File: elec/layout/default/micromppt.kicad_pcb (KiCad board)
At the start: 2 copper layers, 25.7 x 15.1 mm, 20 parts, among them U5 10µF ±10% 10V X5R, U6 10kΩ ±1% 62.5mW

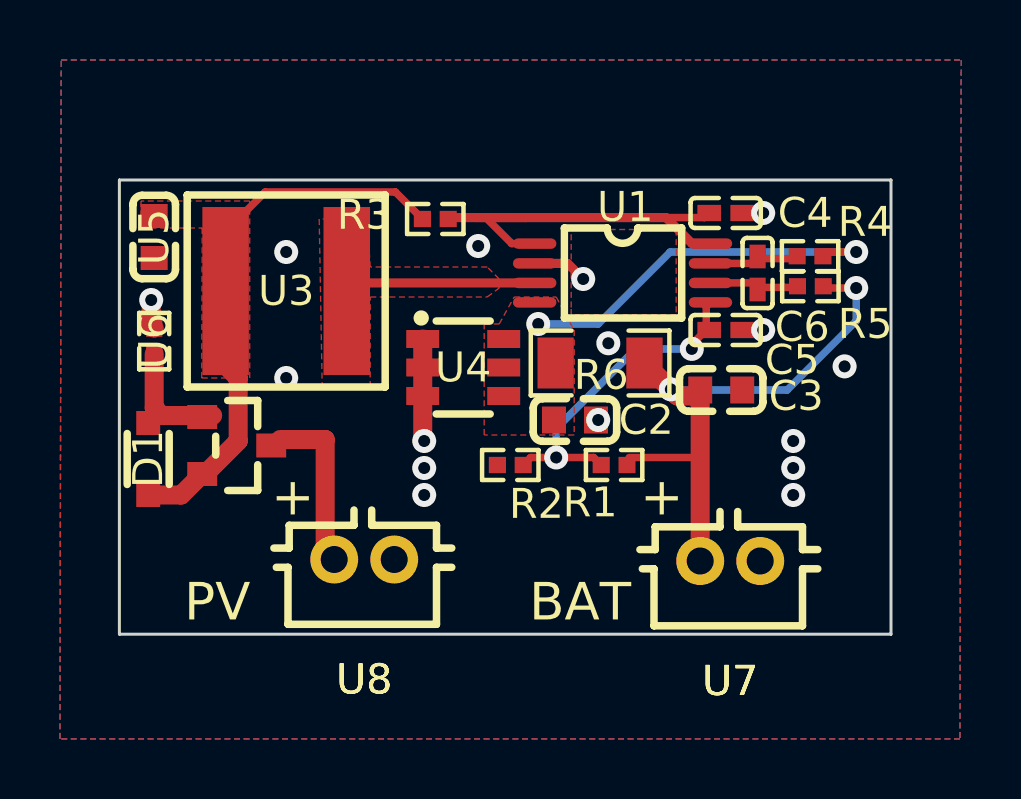
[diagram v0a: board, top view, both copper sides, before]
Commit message: fixed .github/workflows/ci.yml and set github actions versions to v4
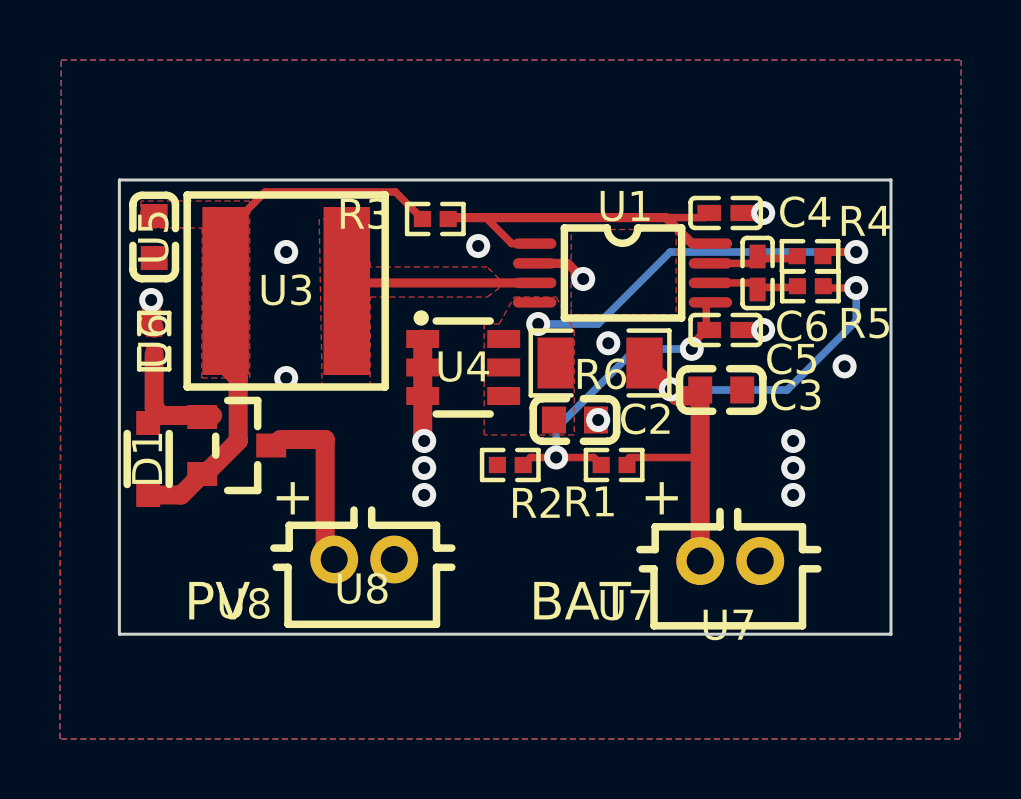
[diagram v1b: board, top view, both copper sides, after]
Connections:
- net S renamed C
- net VOUT renamed cathode
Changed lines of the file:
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@@
     (net 3 "ICTRL_PLUS")
     (net 4 "LX")
-    (net 5 "VOUT")
+    (net 5 "cathode")
     (net 6 "VCTRL")
     (net 7 "G")
-    (net 8 "S")
+    (net 8 "C")
     (net 9 "hv")
     (net 10 "gnd")
@@
             (size 1.1 0.6)
             (layers "F.Cu" "F.Mask" "F.Paste")
-            (net 5 "VOUT")
+            (net 5 "cathode")
             (pintype "stereo")
         )
@@
             (size 1.1 0.6)
             (layers "F.Cu" "F.Mask" "F.Paste")
-            (net 5 "VOUT")
+            (net 5 "cathode")
             (pintype "stereo")
         )
@@
             (size 1.1 0.6)
             (layers "F.Cu" "F.Mask" "F.Paste")
-            (net 5 "VOUT")
+            (net 5 "cathode")
             (pintype "stereo")
         )
@@
         (at 74.6 55.65 180)
         (property "Reference" "U8"
-            (at 0 -4 0)
+            (at 4 -1.5 0)
             (layer "F.SilkS")
             (hide no)
@@
             (layer "F.SilkS")
         )
-        (fp_line
-            (start 3 1.7)
-            (end -3 1.7)
-            (stroke
-                (width 3)
-                (type solid)
-            )
-            (layer "F.Fab")
-        )
-        (fp_line
-            (start 3 -2.8)
-            (end 3 1.7)
-            (stroke
-                (width 3)
-                (type solid)
-            )
-            (layer "F.Fab")
-        )
-        (fp_line
-            (start -3 -2.8)
-            (end 3 -2.8)
-            (stroke
-                (width 3)
-                (type solid)
-            )
-            (layer "F.Fab")
-        )
-        (fp_line
-            (start -3 -2.8)
-            (end -3 -2.8)
-            (stroke
-                (width 3)
-                (type solid)
-            )
-            (layer "F.Fab")
-        )
         (fp_circle
             (center 2.95 -2.8)
@@
         )
         (fp_text user "${REFERENCE}"
-            (at 0 -4 0)
+            (at 0.065 -1 0)
             (layer "F.SilkS")
             (effects
@@
             (size 0.8 0.9)
             (layers "F.Cu" "F.Mask" "F.Paste")
-            (net 8 "S")
+            (net 8 "C")
         )
         (pad "2" smd rect
@@
         (at 86.8 55.7 180)
         (property "Reference" "U7"
-            (at 0 -4 0)
+            (at 3.5 -1.5 0)
             (layer "F.SilkS")
             (hide no)
@@
             (layer "F.SilkS")
         )
-        (fp_line
-            (start 3 1.7)
-            (end -3 1.7)
-            (stroke
-                (width 3)
-                (type solid)
-            )
-            (layer "F.Fab")
-        )
-        (fp_line
-            (start 3 -2.8)
-            (end 3 1.7)
-            (stroke
-                (width 3)
-                (type solid)
-            )
-            (layer "F.Fab")
-        )
-        (fp_line
-            (start -3 -2.8)
-            (end 3 -2.8)
-            (stroke
-                (width 3)
-                (type solid)
-            )
-            (layer "F.Fab")
-        )
-        (fp_line
-            (start -3 -2.8)
-            (end -3 -2.8)
-            (stroke
-                (width 3)
-                (type solid)
-            )
-            (layer "F.Fab")
-        )
         (fp_circle
             (center 2.95 -2.8)
@@
         )
         (fp_text user "${REFERENCE}"
-            (at 0 -4 0)
+            (at 0.065 -2.16 0)
             (layer "F.SilkS")
             (effects
@@
             (size 0.35 1.45)
             (layers "F.Cu" "F.Mask" "F.Paste")
-            (net 5 "VOUT")
+            (net 5 "cathode")
             (pintype "stereo")
         )
@@
             (size 0.8 0.8)
             (layers "F.Cu" "F.Mask" "F.Paste")
-            (net 8 "S")
+            (net 8 "C")
         )
         (pad "2" smd rect
@@
             (size 0.57 0.54)
             (layers "F.Cu" "F.Mask" "F.Paste")
-            (net 5 "VOUT")
+            (net 5 "cathode")
         )
         (embedded_fonts no)
@@
             (size 1.55 5.6)
             (layers "F.Cu" "F.Mask" "F.Paste")
-            (net 8 "S")
+            (net 8 "C")
             (pintype "stereo")
         )
@@
             (size 0.8 0.9)
             (layers "F.Cu" "F.Mask" "F.Paste")
-            (net 5 "VOUT")
+            (net 5 "cathode")
         )
         (pad "2" smd rect
@@
             (size 1.21 1.7)
             (layers "F.Cu" "F.Mask" "F.Paste")
-            (net 5 "VOUT")
+            (net 5 "cathode")
         )
         (pad "2" smd rect
@@
             (size 0.57 0.54)
             (layers "F.Cu" "F.Mask" "F.Paste")
-            (net 8 "S")
+            (net 8 "C")
         )
         (pad "2" smd rect
@@
             (size 1 0.8)
             (layers "F.Cu" "F.Mask" "F.Paste")
-            (net 8 "S")
+            (net 8 "C")
         )
         (pad "3" smd rect
@@
     (zone
         (net 8)
-        (net_name "S")
+        (net_name "C")
         (layers "F.Cu")
         (hatch edge 0.5)
@@
     (zone
         (net 5)
-        (net_name "VOUT")
+        (net_name "cathode")
         (layers "F.Cu")
         (hatch edge 0.5)

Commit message: init
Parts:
- moved U8 4.20 mm to (70.4, 55.7)
- moved R2 2.25 mm to (77.3, 51.8)
- moved R1 1.17 mm to (84.1, 52.2)
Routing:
- net VCTRL: track 11.2 -> 14.5 mm
- net D: track 5.62 -> 4.72 mm
- net hv: track 19.4 -> 18.5 mm
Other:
- board text removed: "{{GITHASH}}"

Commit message: changed layouts to original layout folder name, fixed layout syncing
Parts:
- C2: value 4.7µF ±10% 16V X5R -> 4.7µF ±10% 10V X5R
- C3, U5: value 10µF ±10% 10V X5R -> 10µF ±20% 6.3V X5R
- R2: value 300kΩ ±1% 62.5mW -> 330kΩ ±1% 62.5mW
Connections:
- net cathode renamed VOUT
- D1 pad 1: C -> D
- R3 pad 1: C -> S
- U2 pad 2: C -> S
- U3 pad 1: C -> S
- U5 pad 1: C -> S
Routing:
- net S: track 0.00 -> 21.9 mm
- net C: track 21.9 -> 0.00 mm
- net D: track 4.72 -> 0.00 mm
- net (no net): track 0.00 -> 4.72 mm
- added copper zone on F.Cu, net S
- removed copper zone on F.Cu, net C

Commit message: added voltage window monitor
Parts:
- removed D1: , lib:SOD-323F_L1.7-W1.3-LS2.5-R-RD
- removed U2: , lib:SOT-23_L2.9-W1.3-P1.90-LS2.4-BR
- removed U6: 10kΩ ±1% 62.5mW, atopile:R0402-56259e
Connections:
- net VOUT renamed cathode
- C3 pad 1: hv -> hv-1
- R1 pad 1: hv -> hv-1
- R3 pad 1: S -> hv
- R5 pad 2: hv -> hv-1
- R6 pad 2: hv -> hv-1
- U3 pad 1: S -> hv
- U5 pad 1: S -> hv
- U7 pad 1: hv -> hv-1
- U8 pad 1: D -> hv
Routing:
- net S: track 21.9 -> 0.00 mm
- net hv-1: track 0.00 -> 18.5 mm, vias 0 -> 2
- net (no net): track 4.72 -> 0.00 mm
- net G: track 3.85 -> 0.00 mm
- net hv: track 18.5 -> 17.5 mm, vias 2 -> 0
- removed copper zone on F.Cu, net S

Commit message: fixed
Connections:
- C3 pad 1: hv-1 -> hv
- R1 pad 1: hv-1 -> hv
- R3 pad 1: hv -> hv-1
- R5 pad 2: hv-1 -> hv
- R6 pad 2: hv-1 -> hv
- U3 pad 1: hv -> hv-1
- U5 pad 1: hv -> hv-1
- U7 pad 1: hv-1 -> hv
- U8 pad 1: hv -> hv-1
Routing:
- net hv-1: track 18.5 -> 17.5 mm, vias 2 -> 0
- net hv: track 17.5 -> 18.5 mm, vias 0 -> 2
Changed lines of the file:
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@@
     (net 5 "cathode")
     (net 6 "VCTRL")
-    (net 7 "hv-1")
+    (net 7 "hv")
     (net 8 "gnd")
-    (net 9 "hv")
+    (net 9 "hv-1")
     (footprint "lib:SOT-23-6_L2.9-W1.6-P0.95-LS2.8-BR"
         (layer "F.Cu")
@@
             (size 0.57 0.54)
             (layers "F.Cu" "F.Mask" "F.Paste")
-            (net 7 "hv-1")
+            (net 7 "hv")
         )
         (pad "2" smd rect
@@
             (drill 0.900024)
             (layers "*.Cu" "*.Mask")
-            (net 9 "hv")
+            (net 9 "hv-1")
             (remove_unused_layers no)
         )
@@
             (size 0.8 0.9)
             (layers "F.Cu" "F.Mask" "F.Paste")
-            (net 9 "hv")
+            (net 9 "hv-1")
         )
         (pad "2" smd rect
@@
             (drill 0.900024)
             (layers "*.Cu" "*.Mask")
-            (net 7 "hv-1")
+            (net 7 "hv")
             (remove_unused_layers no)
         )
@@
             (size 0.57 0.54)
             (layers "F.Cu" "F.Mask" "F.Paste")
-            (net 7 "hv-1")
+            (net 7 "hv")
         )
         (embedded_fonts no)
@@
             (size 1.55 5.6)
             (layers "F.Cu" "F.Mask" "F.Paste")
-            (net 9 "hv")
+            (net 9 "hv-1")
             (pintype "stereo")
         )
@@
             (size 1.21 1.7)
             (layers "F.Cu" "F.Mask" "F.Paste")
-            (net 7 "hv-1")
+            (net 7 "hv")
         )
         (embedded_fonts no)
@@
             (size 0.8 0.9)
             (layers "F.Cu" "F.Mask" "F.Paste")
-            (net 7 "hv-1")
+            (net 7 "hv")
         )
         (pad "2" smd rect
@@
             (size 0.57 0.54)
             (layers "F.Cu" "F.Mask" "F.Paste")
-            (net 9 "hv")
+            (net 9 "hv-1")
         )
         (pad "2" smd rect

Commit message: ready for publishing on the ato repo
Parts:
- moved U5 6.94 mm to (69.2, 51.6)
- moved U8 4.18 mm to (73.2, 52.6)
- moved U7 3.90 mm to (89.1, 52.5)
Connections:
- net cathode renamed VOUT
- C3 pad 1: hv -> hv-1
- R1 pad 1: hv -> hv-1
- R3 pad 1: hv-1 -> hv
- R5 pad 2: hv -> hv-1
- R6 pad 2: hv -> hv-1
- U3 pad 1: hv-1 -> hv
- U5 pad 1: hv-1 -> hv
- U7 pad 1: hv -> hv-1
- U8 pad 1: hv-1 -> hv
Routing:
- net hv: track 18.5 -> 29.2 mm, vias 2 -> 0
- net gnd: track 6.29 -> 5.31 mm, vias 16 -> 14
- net hv-1: track 17.5 -> 17.4 mm, vias 0 -> 2
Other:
- board size 25.7 x 15.1 mm -> 23.9 x 12 mm

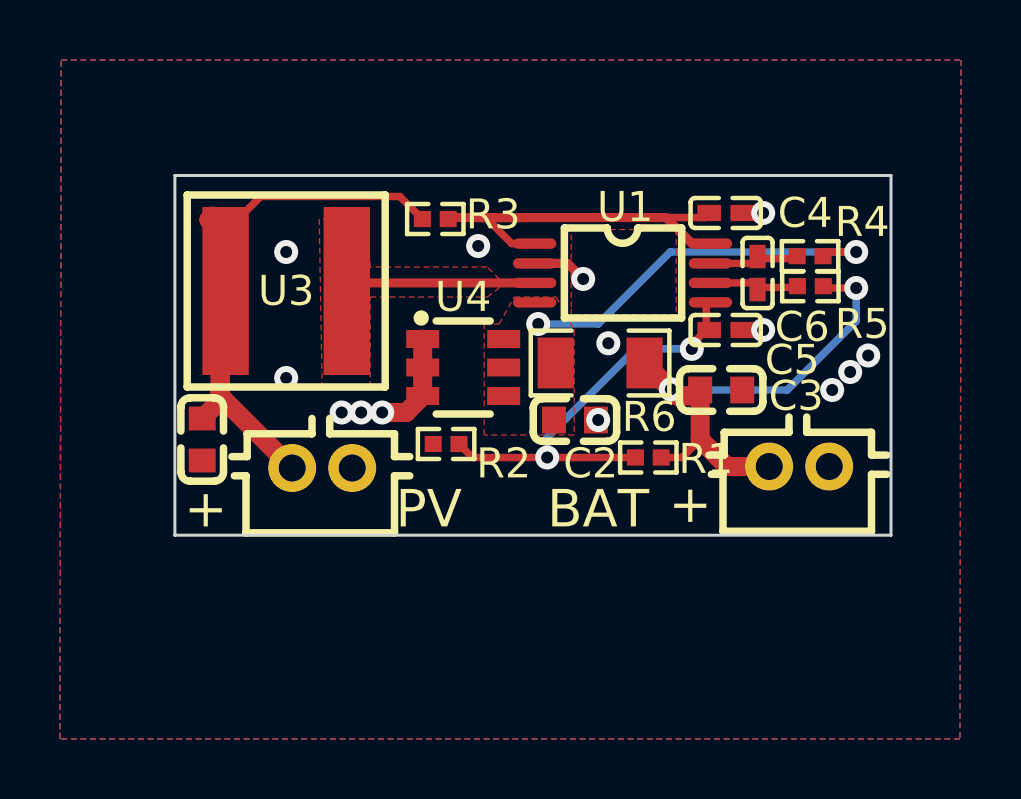
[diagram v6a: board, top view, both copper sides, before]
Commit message: added load output and BPC
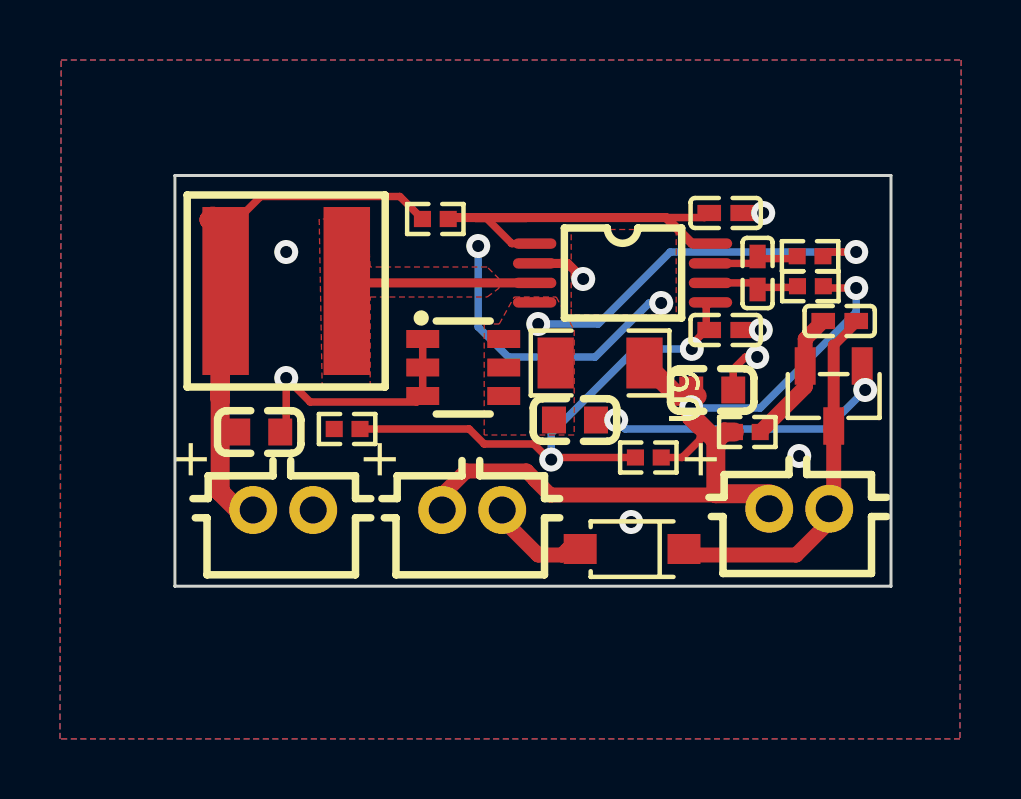
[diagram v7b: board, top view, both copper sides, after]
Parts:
- added D1: , atopile:SOD-123F_L2.7-W1.6-LS3.8-RD-1-139753, F.Cu at (83.5, 55.3)
- added U10: , lib:CONN-TH_B2B-PH-K-S, F.Cu at (78.2, 54.0)
- added U2: 100nF ±10% 16V X7R, atopile:C0402-b3ef17, F.Cu at (90.5, 47.7)
- added U6: 100Ω ±1% 62.5mW, atopile:R0402-56259e, F.Cu at (87.4, 51.4)
- added U9: , atopile:SOT-23-3_L2.9-W1.3-P1.90-LS2.4-BR-688f29, F.Cu at (90.2, 50.2)
- C3, U5: value 10µF ±20% 6.3V X5R -> 10µF ±10% 10V X5R
- R2: value 330kΩ ±1% 62.5mW -> 300kΩ ±1% 62.5mW
- moved R2 3.34 mm to (74.0, 51.3)
- moved U5 1.92 mm to (71.1, 51.4), turned to 0 degrees
- moved U8 1.91 mm to (71.9, 54.0)
- moved U7 1.41 mm to (89.1, 54.0)
- moved C3 0.30 mm to (86.2, 50.0)
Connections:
- U7 pad 2: gnd -> gnd-1
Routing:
- net gnd: track 5.31 -> 33.3 mm, vias 14 -> 12
- net hv-1: track 17.4 -> 33.0 mm
- net gnd-1: track 0.00 -> 12.2 mm
- net VDD: track 0.00 -> 4.57 mm
- net VCTRL: track 14.6 -> 18.2 mm
- net A: track 0.00 -> 3.48 mm
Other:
- board size 23.9 x 12 mm -> 23.9 x 13.7 mm
- board text added: "LOAD"

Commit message: reran DRC
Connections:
- net VOUT renamed cathode
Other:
- board text added: "micromppt v3 lucy moglia 04/21/25"
- board text added: "{{GITHASH}}"
- board text removed: "micromppt lucy moglia 11/29/24"
